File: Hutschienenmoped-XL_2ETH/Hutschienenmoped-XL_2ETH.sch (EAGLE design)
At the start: 127 parts, among them J1 638207222005, J12 61300615721, J13 638207222005, J14 61300815721, J15 638207222008, J2 645004114822, J4 61300421121, J7 638207222005, J8 638207222007, U4 TLE9250VSJ

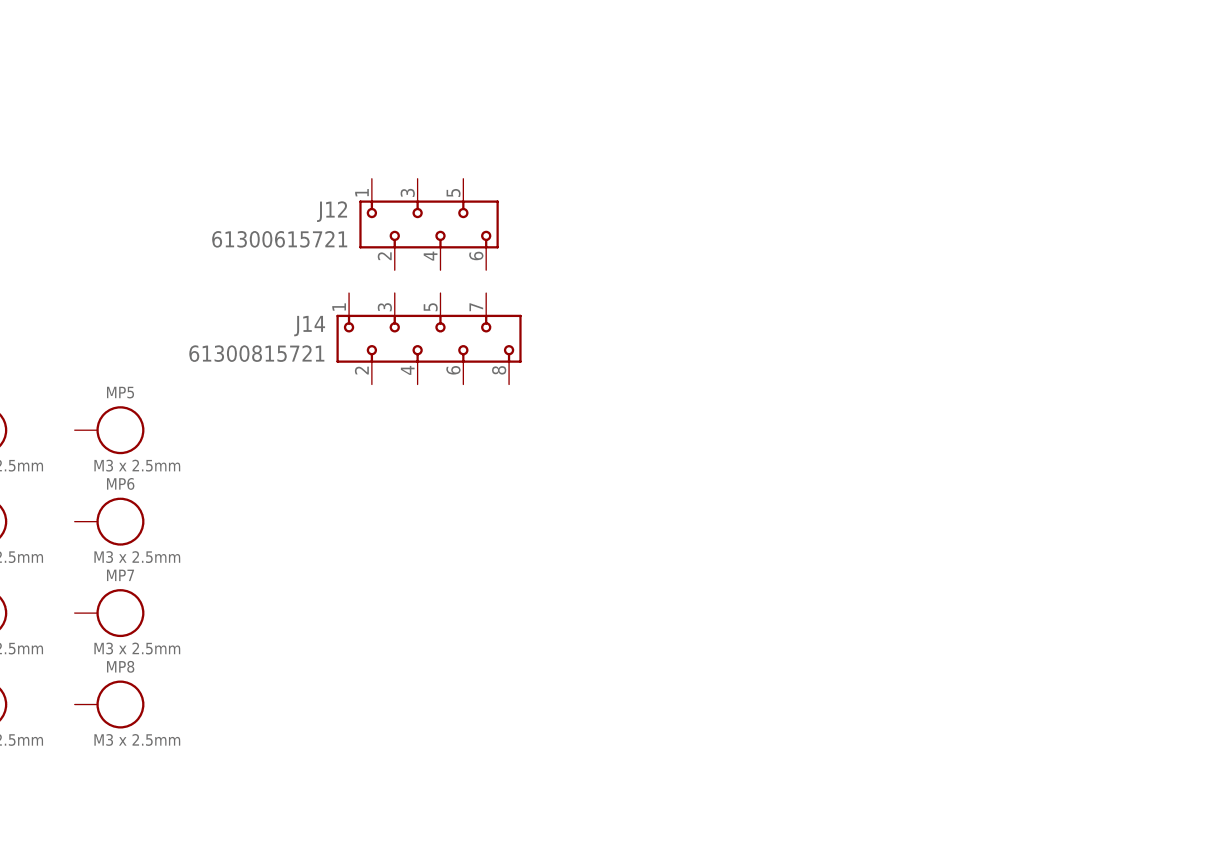
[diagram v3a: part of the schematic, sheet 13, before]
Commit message: Update grid distance in board file and rename connector elements: - Changed grid distance from 6mm to 22.86mm for better alignment. - Renamed connector elements J12, J14 to W1-J2, W1-J1 respectively. - Added new connector elements W2-J2, W2-J1 with updated positions.
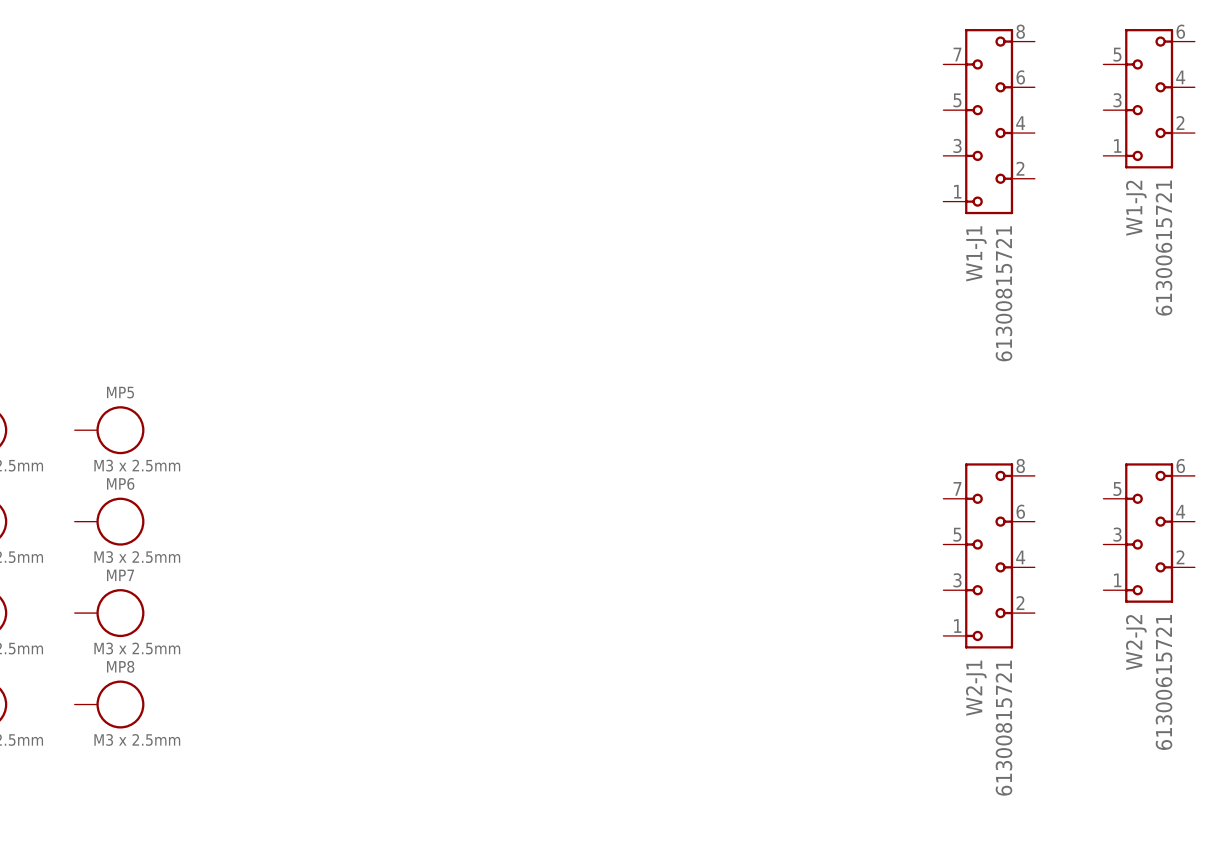
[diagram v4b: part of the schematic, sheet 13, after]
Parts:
- removed J12: 61300615721, Wurth_Connectors_WR-PHD:6130XX15721_61300615721
- removed J14: 61300815721, Wurth_Connectors_WR-PHD:6130XX15721_61300815721
- added W1-J1, W2-J1: 61300815721, Wurth_Connectors_WR-PHD:6130XX15721_61300815721
- added W1-J2, W2-J2: 61300615721, Wurth_Connectors_WR-PHD:6130XX15721_61300615721
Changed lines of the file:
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@@
 <part name="MP3" library="Wurth_Assembly_WA-SMSI" library_urn="urn:adsk.eagle:library:14418591" deviceset="WA-SMSI_9774XXX360" device="_9774025360R" package3d_urn="urn:adsk.eagle:package:14321862/4" value="M3 x 2.5mm"/>
 <part name="MP4" library="Wurth_Assembly_WA-SMSI" library_urn="urn:adsk.eagle:library:14418591" deviceset="WA-SMSI_9774XXX360" device="_9774025360R" package3d_urn="urn:adsk.eagle:package:14321862/4" value="M3 x 2.5mm"/>
-<part name="J12" library="Wurth_Connectors_WR-PHD" library_urn="urn:adsk.eagle:library:14804658" deviceset="6130XX15721_61300615721" device="" package3d_urn="urn:adsk.eagle:package:14805618/2" value=" 61300615721 "/>
-<part name="J14" library="Wurth_Connectors_WR-PHD" library_urn="urn:adsk.eagle:library:14804658" deviceset="6130XX15721_61300815721" device="" package3d_urn="urn:adsk.eagle:package:14805619/2" value=" 61300815721 "/>
+<part name="W1-J2" library="Wurth_Connectors_WR-PHD" library_urn="urn:adsk.eagle:library:14804658" deviceset="6130XX15721_61300615721" device="" package3d_urn="urn:adsk.eagle:package:14805618/2" value=" 61300615721 "/>
+<part name="W1-J1" library="Wurth_Connectors_WR-PHD" library_urn="urn:adsk.eagle:library:14804658" deviceset="6130XX15721_61300815721" device="" package3d_urn="urn:adsk.eagle:package:14805619/2" value=" 61300815721 "/>
 <part name="+3V3" library="supply1" library_urn="urn:adsk.eagle:library:371" deviceset="+3V3" device=""/>
 <part name="ECU_GND30" library="supply_isobus" deviceset="ECU_GND" device=""/>
@@
 <part name="MP7" library="Wurth_Assembly_WA-SMSI" library_urn="urn:adsk.eagle:library:14418591" deviceset="WA-SMSI_9774XXX360" device="_9774025360R" package3d_urn="urn:adsk.eagle:package:14321862/4" value="M3 x 2.5mm"/>
 <part name="MP8" library="Wurth_Assembly_WA-SMSI" library_urn="urn:adsk.eagle:library:14418591" deviceset="WA-SMSI_9774XXX360" device="_9774025360R" package3d_urn="urn:adsk.eagle:package:14321862/4" value="M3 x 2.5mm"/>
+<part name="W2-J2" library="Wurth_Connectors_WR-PHD" library_urn="urn:adsk.eagle:library:14804658" deviceset="6130XX15721_61300615721" device="" package3d_urn="urn:adsk.eagle:package:14805618/2" value=" 61300615721 "/>
+<part name="W2-J1" library="Wurth_Connectors_WR-PHD" library_urn="urn:adsk.eagle:library:14804658" deviceset="6130XX15721_61300815721" device="" package3d_urn="urn:adsk.eagle:package:14805619/2" value=" 61300815721 "/>
 </parts>
 <sheets>
@@
 <attribute name="VALUE" x="62.992" y="84.328" size="1.27" layer="95"/>
 </instance>
-<instance part="J12" gate="G$1" x="114.3" y="142.24" smashed="yes">
-<attribute name="NAME" x="106.68" y="143.002" size="1.778" layer="95" align="bottom-right"/>
-<attribute name="VALUE" x="106.68" y="139.7" size="1.778" layer="96" align="bottom-right"/>
-</instance>
-<instance part="J14" gate="G$1" x="114.3" y="129.54" smashed="yes">
-<attribute name="NAME" x="104.14" y="130.302" size="1.778" layer="95" align="bottom-right"/>
-<attribute name="VALUE" x="104.14" y="127" size="1.778" layer="96" align="bottom-right"/>
+<instance part="W1-J2" gate="G$1" x="195.58" y="154.94" smashed="yes" rot="R90">
+<attribute name="NAME" x="194.818" y="147.32" size="1.778" layer="95" rot="R90" align="bottom-right"/>
+<attribute name="VALUE" x="198.12" y="147.32" size="1.778" layer="96" rot="R90" align="bottom-right"/>
+</instance>
+<instance part="W1-J1" gate="G$1" x="177.8" y="152.4" smashed="yes" rot="R90">
+<attribute name="NAME" x="177.038" y="142.24" size="1.778" layer="95" rot="R90" align="bottom-right"/>
+<attribute name="VALUE" x="180.34" y="142.24" size="1.778" layer="96" rot="R90" align="bottom-right"/>
 </instance>
 <instance part="MP5" gate="G$1" x="81.28" y="119.38" smashed="yes">
@@
 <attribute name="VALUE" x="78.232" y="84.328" size="1.27" layer="95"/>
 </instance>
+<instance part="W2-J2" gate="G$1" x="195.58" y="106.68" smashed="yes" rot="R90">
+<attribute name="NAME" x="194.818" y="99.06" size="1.778" layer="95" rot="R90" align="bottom-right"/>
+<attribute name="VALUE" x="198.12" y="99.06" size="1.778" layer="96" rot="R90" align="bottom-right"/>
+</instance>
+<instance part="W2-J1" gate="G$1" x="177.8" y="104.14" smashed="yes" rot="R90">
+<attribute name="NAME" x="177.038" y="93.98" size="1.778" layer="95" rot="R90" align="bottom-right"/>
+<attribute name="VALUE" x="180.34" y="93.98" size="1.778" layer="96" rot="R90" align="bottom-right"/>
+</instance>
 </instances>

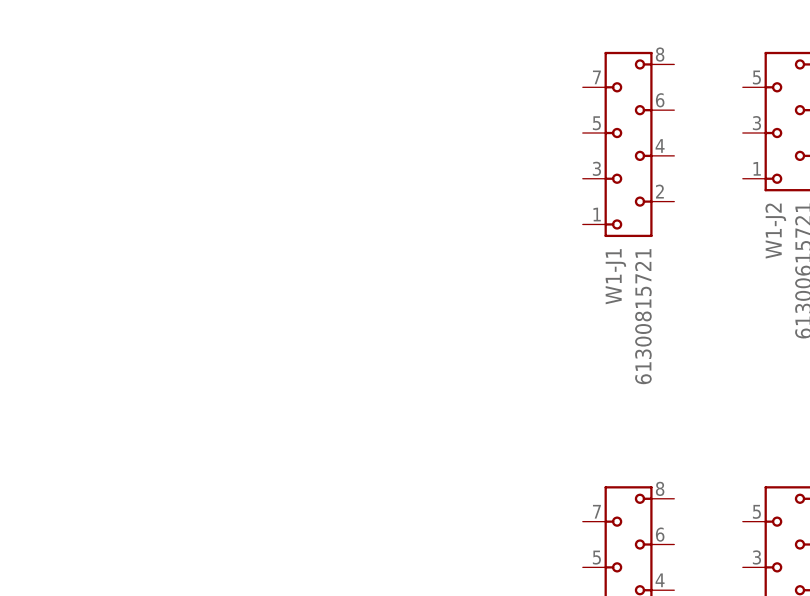
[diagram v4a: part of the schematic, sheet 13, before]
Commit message: Update grid settings, change font display, adjust pad sizes and hole drills, add new package with 10-pin socket header, modify parameter values for pads and vias. Add symbol for 10-pin socket header THT.
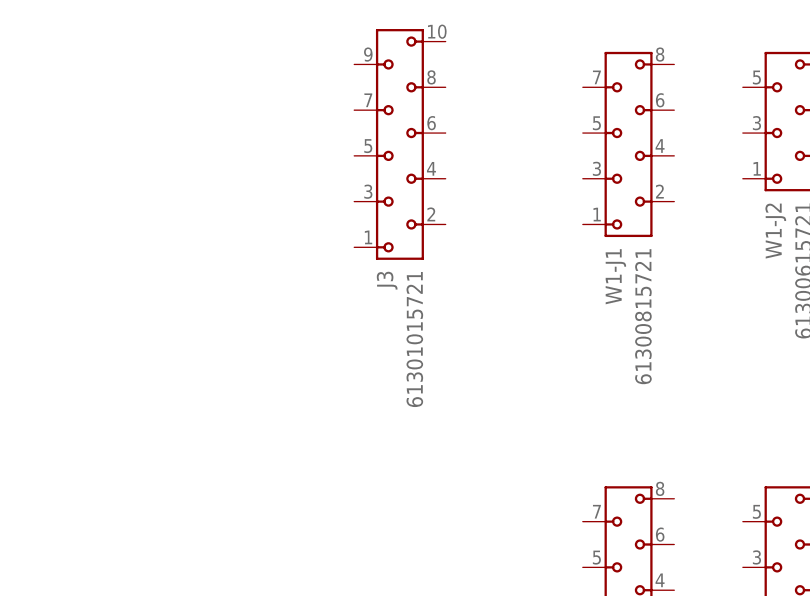
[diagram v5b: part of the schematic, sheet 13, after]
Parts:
- added J3: 61301015721, Wurth_Connectors_WR-PHD:6130XX15721_61301015721
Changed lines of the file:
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@@
 <part name="W2-J2" library="Wurth_Connectors_WR-PHD" library_urn="urn:adsk.eagle:library:14804658" deviceset="6130XX15721_61300615721" device="" package3d_urn="urn:adsk.eagle:package:14805618/2" value=" 61300615721 "/>
 <part name="W2-J1" library="Wurth_Connectors_WR-PHD" library_urn="urn:adsk.eagle:library:14804658" deviceset="6130XX15721_61300815721" device="" package3d_urn="urn:adsk.eagle:package:14805619/2" value=" 61300815721 "/>
+<part name="J3" library="Wurth_Connectors_WR-PHD" library_urn="urn:adsk.eagle:library:14804658" deviceset="6130XX15721_61301015721" device="" package3d_urn="urn:adsk.eagle:package:14805620/2" value=" 61301015721 "/>
 </parts>
 <sheets>
@@
 <attribute name="VALUE" x="180.34" y="93.98" size="1.778" layer="96" rot="R90" align="bottom-right"/>
 </instance>
+<instance part="J3" gate="G$1" x="152.4" y="152.4" smashed="yes" rot="R90">
+<attribute name="NAME" x="151.638" y="139.7" size="1.778" layer="95" rot="R90" align="bottom-right"/>
+<attribute name="VALUE" x="154.94" y="139.7" size="1.778" layer="96" rot="R90" align="bottom-right"/>
+</instance>
 </instances>

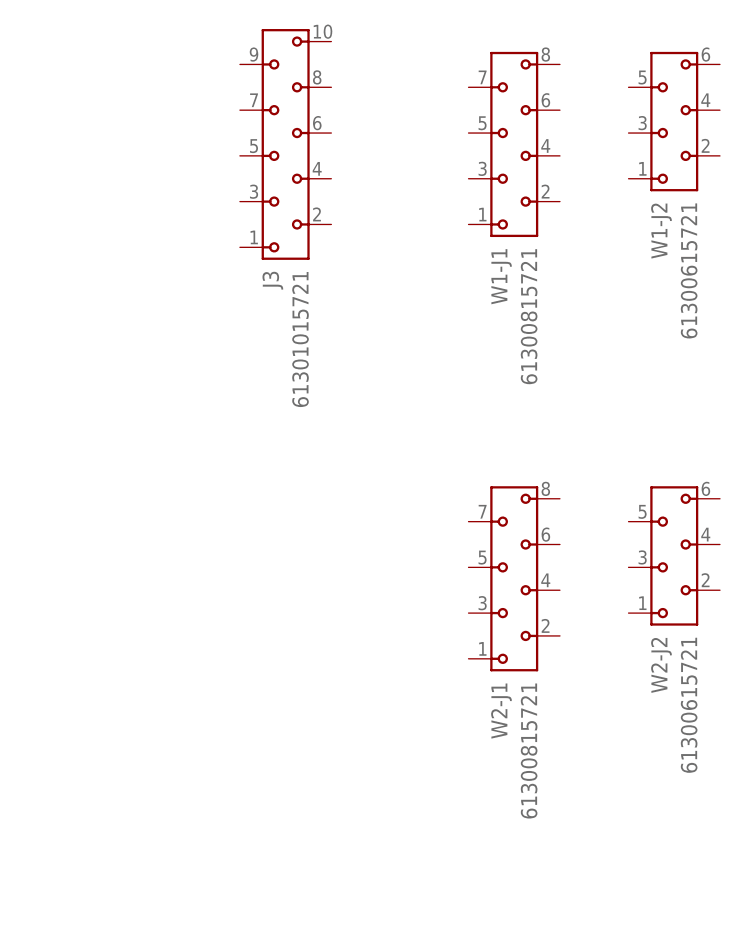
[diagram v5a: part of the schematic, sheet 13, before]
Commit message: Update layer visibility settings for various elements.
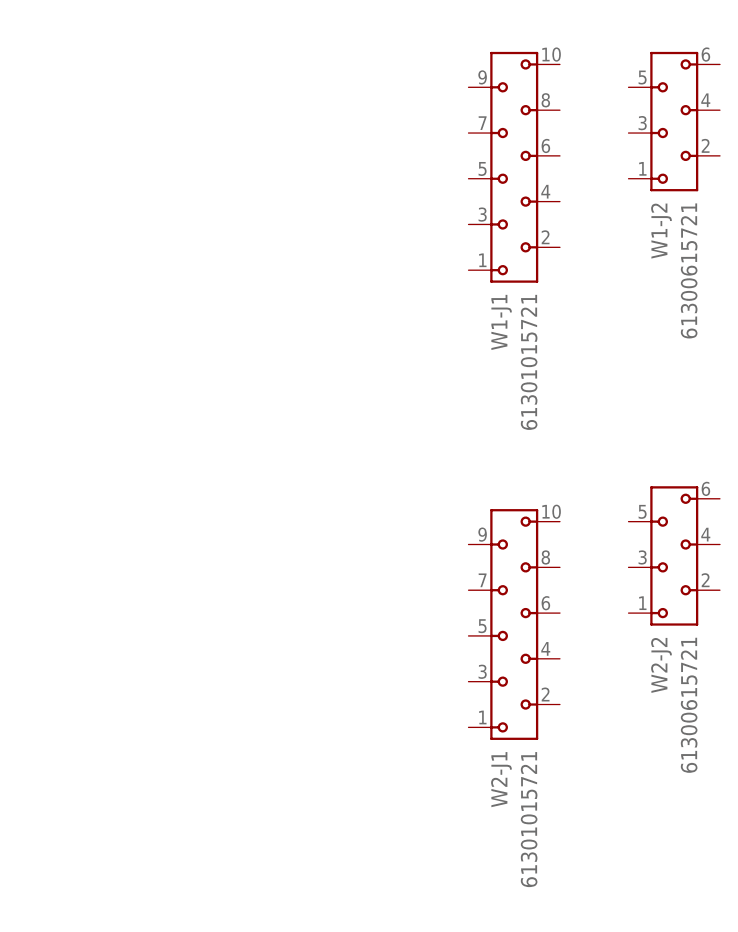
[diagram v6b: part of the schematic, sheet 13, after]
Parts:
- removed J3: 61301015721, Wurth_Connectors_WR-PHD:6130XX15721_61301015721
- W1-J1, W2-J1: value 61300815721 -> 61301015721; device Wurth_Connectors_WR-PHD:6130XX15721_61300815721 -> WE-special:6130XX15721_61301015721
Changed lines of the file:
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@@
 <part name="MP4" library="Wurth_Assembly_WA-SMSI" library_urn="urn:adsk.eagle:library:14418591" deviceset="WA-SMSI_9774XXX360" device="_9774025360R" package3d_urn="urn:adsk.eagle:package:14321862/4" value="M3 x 2.5mm"/>
 <part name="W1-J2" library="Wurth_Connectors_WR-PHD" library_urn="urn:adsk.eagle:library:14804658" deviceset="6130XX15721_61300615721" device="" package3d_urn="urn:adsk.eagle:package:14805618/2" value=" 61300615721 "/>
-<part name="W1-J1" library="Wurth_Connectors_WR-PHD" library_urn="urn:adsk.eagle:library:14804658" deviceset="6130XX15721_61300815721" device="" package3d_urn="urn:adsk.eagle:package:14805619/2" value=" 61300815721 "/>
 <part name="+3V3" library="supply1" library_urn="urn:adsk.eagle:library:371" deviceset="+3V3" device=""/>
 <part name="ECU_GND30" library="supply_isobus" deviceset="ECU_GND" device=""/>
@@
 <part name="MP8" library="Wurth_Assembly_WA-SMSI" library_urn="urn:adsk.eagle:library:14418591" deviceset="WA-SMSI_9774XXX360" device="_9774025360R" package3d_urn="urn:adsk.eagle:package:14321862/4" value="M3 x 2.5mm"/>
 <part name="W2-J2" library="Wurth_Connectors_WR-PHD" library_urn="urn:adsk.eagle:library:14804658" deviceset="6130XX15721_61300615721" device="" package3d_urn="urn:adsk.eagle:package:14805618/2" value=" 61300615721 "/>
-<part name="W2-J1" library="Wurth_Connectors_WR-PHD" library_urn="urn:adsk.eagle:library:14804658" deviceset="6130XX15721_61300815721" device="" package3d_urn="urn:adsk.eagle:package:14805619/2" value=" 61300815721 "/>
-<part name="J3" library="Wurth_Connectors_WR-PHD" library_urn="urn:adsk.eagle:library:14804658" deviceset="6130XX15721_61301015721" device="" package3d_urn="urn:adsk.eagle:package:14805620/2" value=" 61301015721 "/>
+<part name="W2-J1" library="WE-special" deviceset="6130XX15721_61301015721" device="" package3d_urn="urn:adsk.eagle:package:14805620/2" value=" 61301015721 "/>
+<part name="W1-J1" library="WE-special" deviceset="6130XX15721_61301015721" device="" package3d_urn="urn:adsk.eagle:package:14805620/2" value=" 61301015721 "/>
 </parts>
 <sheets>
@@
 <attribute name="VALUE" x="198.12" y="147.32" size="1.778" layer="96" rot="R90" align="bottom-right"/>
 </instance>
-<instance part="W1-J1" gate="G$1" x="177.8" y="152.4" smashed="yes" rot="R90">
-<attribute name="NAME" x="177.038" y="142.24" size="1.778" layer="95" rot="R90" align="bottom-right"/>
-<attribute name="VALUE" x="180.34" y="142.24" size="1.778" layer="96" rot="R90" align="bottom-right"/>
-</instance>
 <instance part="MP5" gate="G$1" x="81.28" y="119.38" smashed="yes">
 <attribute name="NAME" x="81.28" y="122.936" size="1.27" layer="95" align="bottom-center"/>
@@
 <attribute name="VALUE" x="198.12" y="99.06" size="1.778" layer="96" rot="R90" align="bottom-right"/>
 </instance>
-<instance part="W2-J1" gate="G$1" x="177.8" y="104.14" smashed="yes" rot="R90">
-<attribute name="NAME" x="177.038" y="93.98" size="1.778" layer="95" rot="R90" align="bottom-right"/>
-<attribute name="VALUE" x="180.34" y="93.98" size="1.778" layer="96" rot="R90" align="bottom-right"/>
-</instance>
-<instance part="J3" gate="G$1" x="152.4" y="152.4" smashed="yes" rot="R90">
-<attribute name="NAME" x="151.638" y="139.7" size="1.778" layer="95" rot="R90" align="bottom-right"/>
-<attribute name="VALUE" x="154.94" y="139.7" size="1.778" layer="96" rot="R90" align="bottom-right"/>
+<instance part="W2-J1" gate="G$1" x="177.8" y="99.06" smashed="yes" rot="R90">
+<attribute name="NAME" x="177.038" y="86.36" size="1.778" layer="95" rot="R90" align="bottom-right"/>
+<attribute name="VALUE" x="180.34" y="86.36" size="1.778" layer="96" rot="R90" align="bottom-right"/>
+</instance>
+<instance part="W1-J1" gate="G$1" x="177.8" y="149.86" smashed="yes" rot="R90">
+<attribute name="NAME" x="177.038" y="137.16" size="1.778" layer="95" rot="R90" align="bottom-right"/>
+<attribute name="VALUE" x="180.34" y="137.16" size="1.778" layer="96" rot="R90" align="bottom-right"/>
 </instance>
 </instances>
